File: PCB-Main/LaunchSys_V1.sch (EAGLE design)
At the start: 4 parts

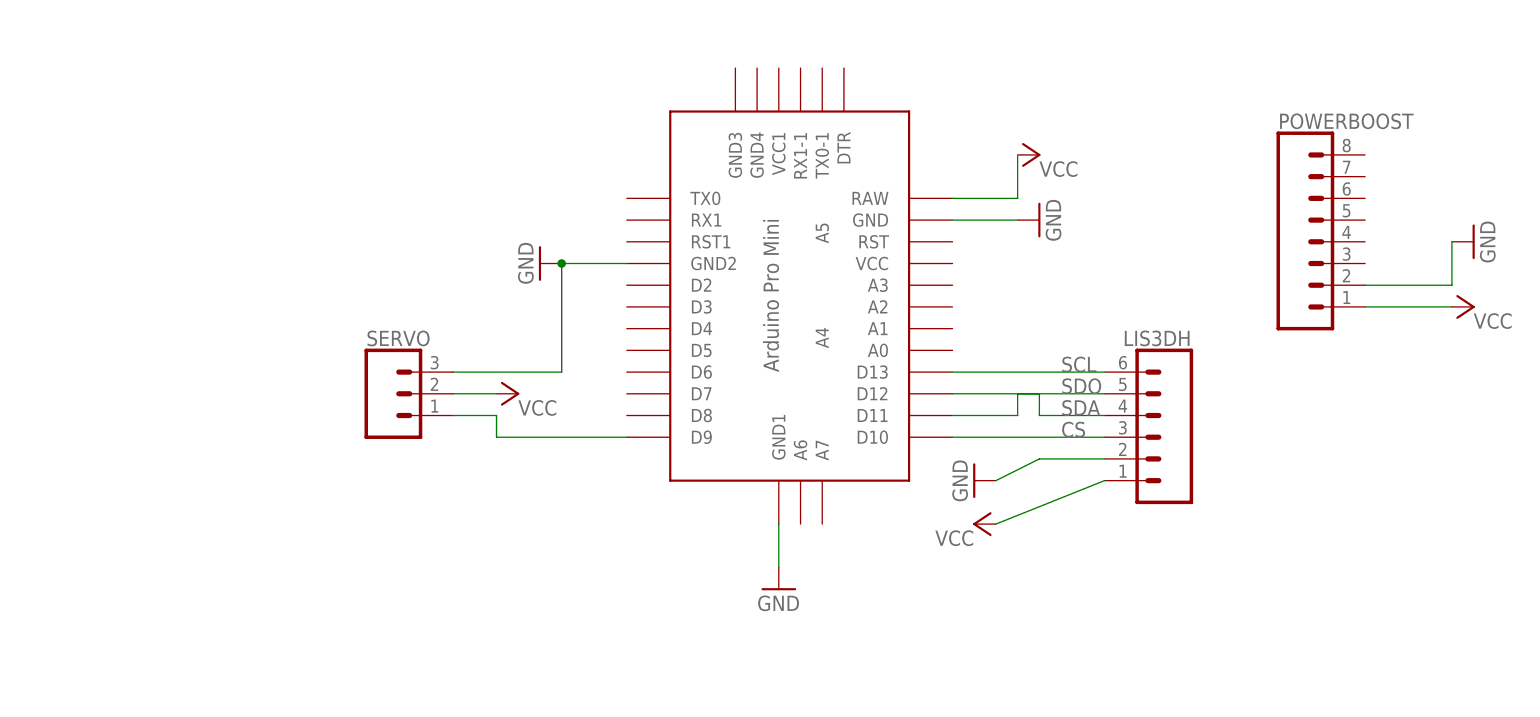
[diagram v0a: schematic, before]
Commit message: Updated launch board to include TIP120 power transistor and switch for controlling solenoid
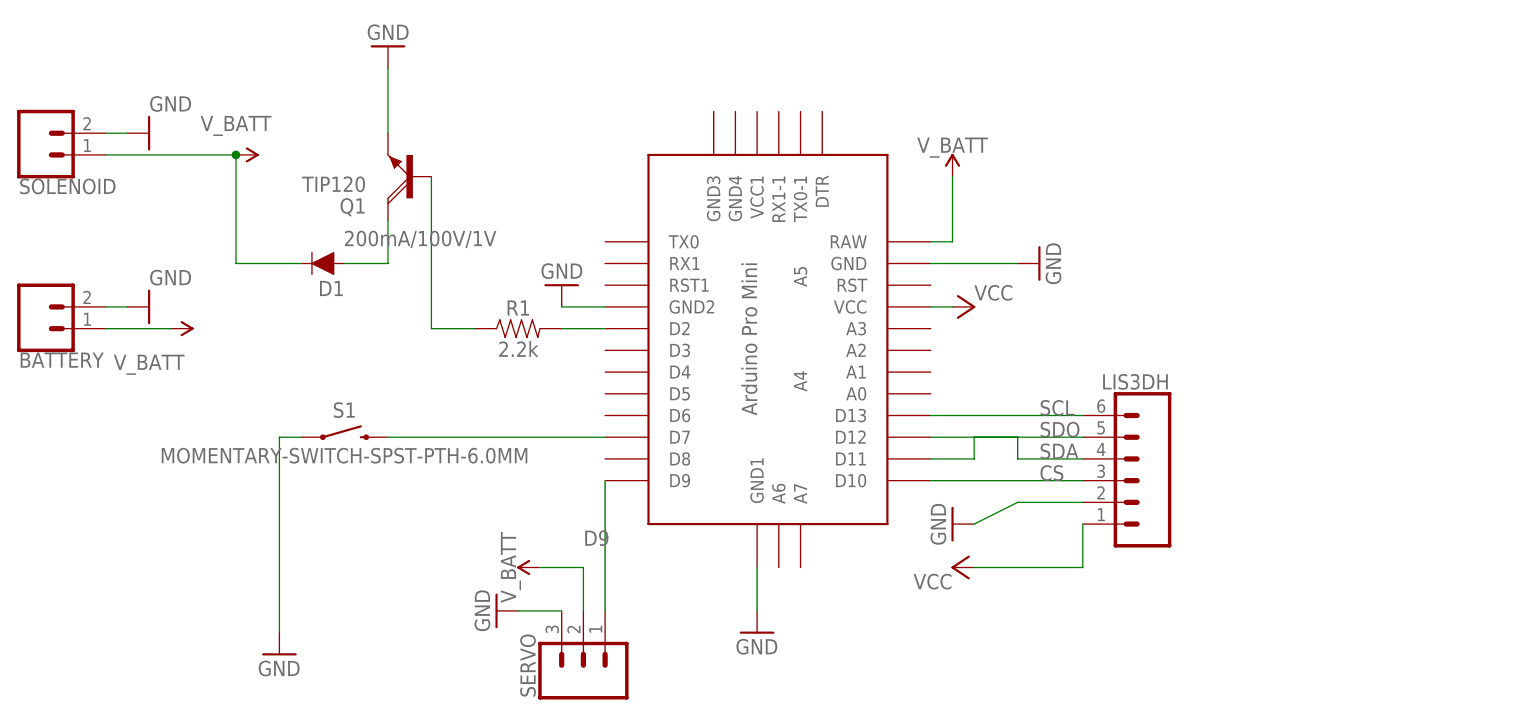
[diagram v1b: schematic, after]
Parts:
- removed POWERBOOST: (no value), SparkFun-Connectors:CONN_08"
- added BATTERY, SOLENOID: (no value), SparkFun-Connectors:CONN_02
- added D1: 200mA/100V/1V, SparkFun-DiscreteSemi:DIODE-1N4148
- added Q1: TIP120, transistor-power:TIP120
- added R1: 2.2k, SparkFun-Resistors:100KOHM-HORIZ-1/4W-5%
- added S1: MOMENTARY-SWITCH-SPST-PTH-6.0MM, SparkFun-Switches:MOMENTARY-SWITCH-SPST-PTH-6.0MM
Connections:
- net N$5 renamed D9
- new net N$1: R1.2, U$1.D2
- new net N$2: Q1.B, R1.1
- new net N$3: S1.2, U$1.D7
- new net N$4: D1.A, Q1.C
- new net V_BATT: BATTERY.1, D1.C, SERVO.2, SOLENOID.1, U$1.RAW
- net GND: now also BATTERY.2, Q1.E, S1.1, SOLENOID.2; no longer POWERBOOST.2
- net VCC: now also U$1.VCC; no longer POWERBOOST.1, SERVO.2, U$1.RAW
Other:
- moved on the sheet: LIS3DH, SERVO
